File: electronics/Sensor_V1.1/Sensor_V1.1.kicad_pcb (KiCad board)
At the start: 2 copper layers, 45.9 x 25.6 mm, 34 parts, among them J1 nuclone_small_left, J2 nuclone_small_right, J5 DevBoardUartInput, Q1 DMG1012, Q2 DMG1012, Q3 DMG1012, U1 PPG_sensor, U2 reference_sot23-3, U3 MCP6541

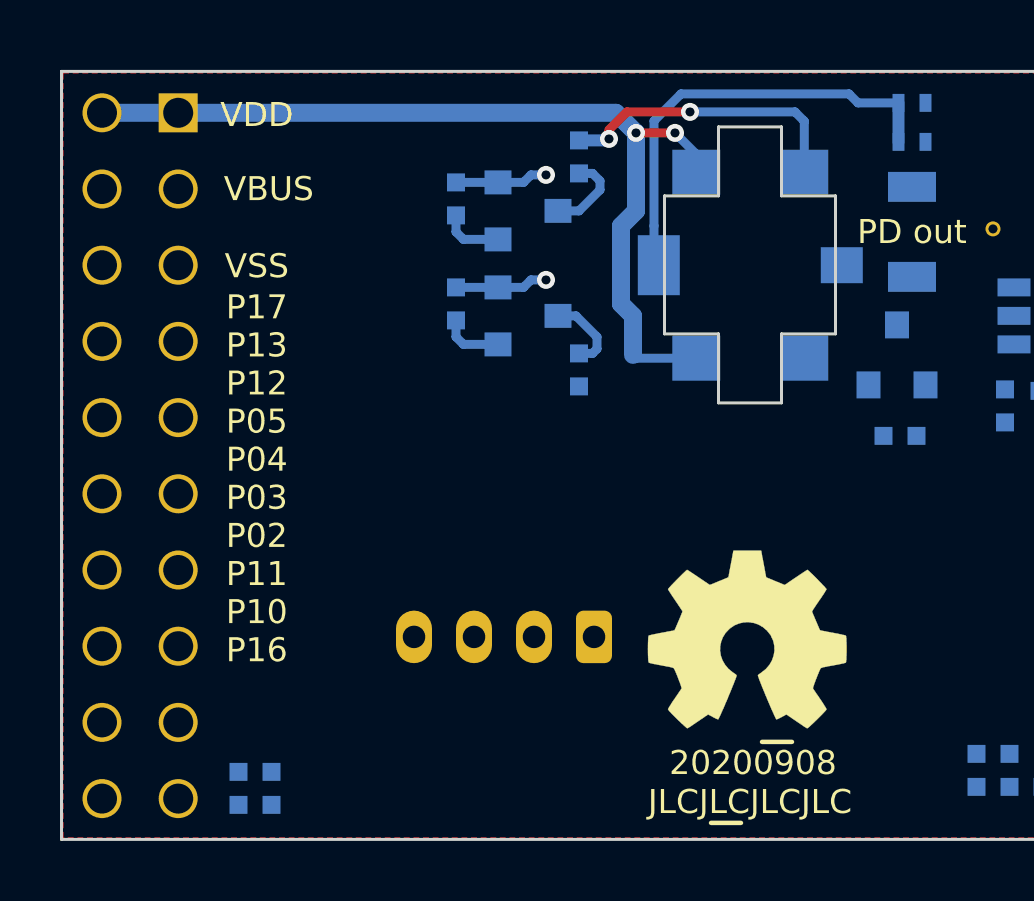
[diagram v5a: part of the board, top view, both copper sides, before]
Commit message: updated layout and started with starground/VDDA
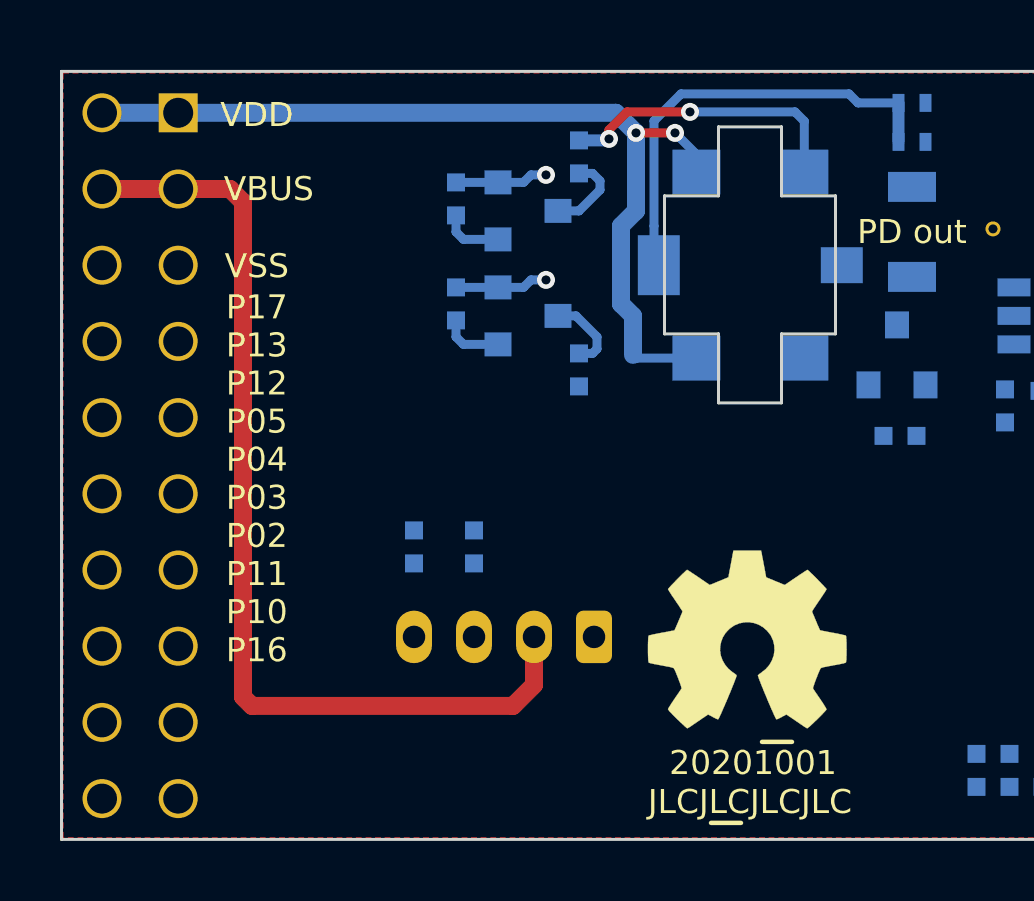
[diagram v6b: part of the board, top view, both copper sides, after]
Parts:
- N2: value 20200908 -> 20201001
- moved R2 11.3 mm to (75.9, 89.4), turned to 270 degrees
- moved R1 9.18 mm to (73.9, 89.4), turned to 270 degrees
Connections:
- J2 pad 19: /VDD -> /VDDA
- J2 pad 20: /VDD -> /VDDA
- JP1 pad 1: /VDD -> /VDDA
- R1 pad 2: Net-(J5-Pad3) -> Net-(J5-Pad4)
- R2 pad 2: Net-(J5-Pad4) -> Net-(J5-Pad3)
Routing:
- net /VBUS: track 0.00 -> 33.1 mm
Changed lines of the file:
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@@
     (thickness 1.6)
     (drawings 57)
-    (tracks 59)
+    (tracks 67)
     (zones 0)
     (modules 34)
@@
   )
   (setup
-    (last_trace_width 0.3)
+    (last_trace_width 0.6)
     (user_trace_width 0.15)
     (user_trace_width 0.2)
@@
   )
   (module SquantorRcl:R_0402_hand (layer B.Cu)
-    (at 68.6 98)
+    (at 75.9 89.4 270)
     (descr "Resistor SMD 0402, reflow soldering, Vishay (see dcrcw.pdf)")
     (tags "resistor 0402")
     (attr smd)
-    (fp_text reference R2 (at 2 0) (layer B.SilkS)
-      (effects (font (size 1 1) (thickness 0.15)) (justify mirror))
-    )
-    (fp_text value 100 (at 0 -1.8) (layer B.Fab)
+    (fp_text reference R2 (at 2 0.2 90) (layer B.SilkS)
+      (effects (font (size 1 1) (thickness 0.15)) (justify mirror))
+    )
+    (fp_text value 100 (at 0 -1.8 90) (layer B.Fab)
       (effects (font (size 1 1) (thickness 0.15)) (justify mirror))
     )
@@
     (fp_line (start -0.1 -0.2) (end -0.1 0.2) (layer B.SilkS) (width 0.15))
     (fp_line (start 0 0.2) (end 0 -0.2) (layer B.SilkS) (width 0.15))
-    (pad 2 smd rect (at 0.55 0) (size 0.6 0.6) (layers B.Cu B.Paste B.Mask)
-      (net 6 "Net-(J5-Pad4)"))
-    (pad 1 smd rect (at -0.55 0) (size 0.6 0.6) (layers B.Cu B.Paste B.Mask)
+    (pad 2 smd rect (at 0.55 0 270) (size 0.6 0.6) (layers B.Cu B.Paste B.Mask)
+      (net 7 "Net-(J5-Pad3)"))
+    (pad 1 smd rect (at -0.55 0 270) (size 0.6 0.6) (layers B.Cu B.Paste B.Mask)
       (net 9 /UART_TX))
     (model ${KISYS3DMOD}/Resistor_SMD.3dshapes/R_0402_1005Metric.step
@@
   )
   (module SquantorRcl:R_0402_hand (layer B.Cu)
-    (at 68.6 96.9)
+    (at 73.9 89.4 270)
     (descr "Resistor SMD 0402, reflow soldering, Vishay (see dcrcw.pdf)")
     (tags "resistor 0402")
     (attr smd)
-    (fp_text reference R1 (at 2 0.1) (layer B.SilkS)
-      (effects (font (size 1 1) (thickness 0.15)) (justify mirror))
-    )
-    (fp_text value 100 (at 0 -1.8) (layer B.Fab)
+    (fp_text reference R1 (at 2 -0.1 90) (layer B.SilkS)
+      (effects (font (size 1 1) (thickness 0.15)) (justify mirror))
+    )
+    (fp_text value 100 (at 0 -1.8 90) (layer B.Fab)
       (effects (font (size 1 1) (thickness 0.15)) (justify mirror))
     )
@@
     (fp_line (start -0.1 -0.2) (end -0.1 0.2) (layer B.SilkS) (width 0.15))
     (fp_line (start 0 0.2) (end 0 -0.2) (layer B.SilkS) (width 0.15))
-    (pad 2 smd rect (at 0.55 0) (size 0.6 0.6) (layers B.Cu B.Paste B.Mask)
-      (net 7 "Net-(J5-Pad3)"))
-    (pad 1 smd rect (at -0.55 0) (size 0.6 0.6) (layers B.Cu B.Paste B.Mask)
+    (pad 2 smd rect (at 0.55 0 270) (size 0.6 0.6) (layers B.Cu B.Paste B.Mask)
+      (net 6 "Net-(J5-Pad4)"))
+    (pad 1 smd rect (at -0.55 0 270) (size 0.6 0.6) (layers B.Cu B.Paste B.Mask)
       (net 8 /UART_RX))
     (model ${KISYS3DMOD}/Resistor_SMD.3dshapes/R_0402_1005Metric.step
@@
       (net 11 /PD_BIAS))
     (pad 1 smd rect (at -0.45 0 180) (size 0.4 0.6) (layers B.Cu B.Mask)
-      (net 3 /VDD))
+      (net 4 /VDDA))
     (model Resistors_SMD.3dshapes/R_0402.wrl
       (at (xyz 0 0 0))
@@
       (effects (font (size 1 1) (thickness 0.15)))
     )
-    (fp_text value 20200908 (at 0.8 -0.1) (layer F.SilkS)
+    (fp_text value 20201001 (at 0.8 -0.1) (layer F.SilkS)
       (effects (font (size 0.8 0.8) (thickness 0.15)))
     )
@@
     (fp_line (start -12.7 -1.905) (end -12.065 -2.54) (layer B.SilkS) (width 0.15))
     (pad 20 thru_hole circle (at 11.43 1.27 90) (size 1.3 1.3) (drill 1) (layers *.Cu *.Mask)
-      (net 3 /VDD))
+      (net 4 /VDDA))
     (pad 19 thru_hole circle (at 11.43 -1.27 90) (size 1.3 1.3) (drill 1) (layers *.Cu *.Mask)
-      (net 3 /VDD))
+      (net 4 /VDDA))
     (pad 18 thru_hole circle (at 8.89 1.27 90) (size 1.3 1.3) (drill 1) (layers *.Cu *.Mask)
       (net 2 /VSS))
@@
   (gr_line (start 62.15 99.15) (end 108.05 99.15) (layer Edge.Cuts) (width 0.1))
   (gr_line (start 62.15 73.55) (end 62.15 99.15) (layer Edge.Cuts) (width 0.1))
+  (segment (start 77.9 92.4) (end 77.9 94) (width 0.6) (layer F.Cu) (net 1))
+  (segment (start 77.9 94) (end 77.2 94.7) (width 0.6) (layer F.Cu) (net 1))
+  (segment (start 77.2 94.7) (end 68.5 94.7) (width 0.6) (layer F.Cu) (net 1))
+  (segment (start 68.5 94.7) (end 68.2 94.4) (width 0.6) (layer F.Cu) (net 1))
+  (segment (start 68.2 94.4) (end 68.2 77.9) (width 0.6) (layer F.Cu) (net 1))
+  (segment (start 67.77 77.47) (end 66.04 77.47) (width 0.6) (layer F.Cu) (net 1))
+  (segment (start 68.2 77.9) (end 67.77 77.47) (width 0.6) (layer F.Cu) (net 1))
+  (segment (start 66.04 77.47) (end 63.5 77.47) (width 0.6) (layer F.Cu) (net 1))
   (segment (start 76.7 80.75) (end 77.55 80.75) (width 0.3) (layer B.Cu) (net 2))
   (via (at 78.3 80.5) (size 0.6) (drill 0.3) (layers F.Cu B.Cu) (net 2))

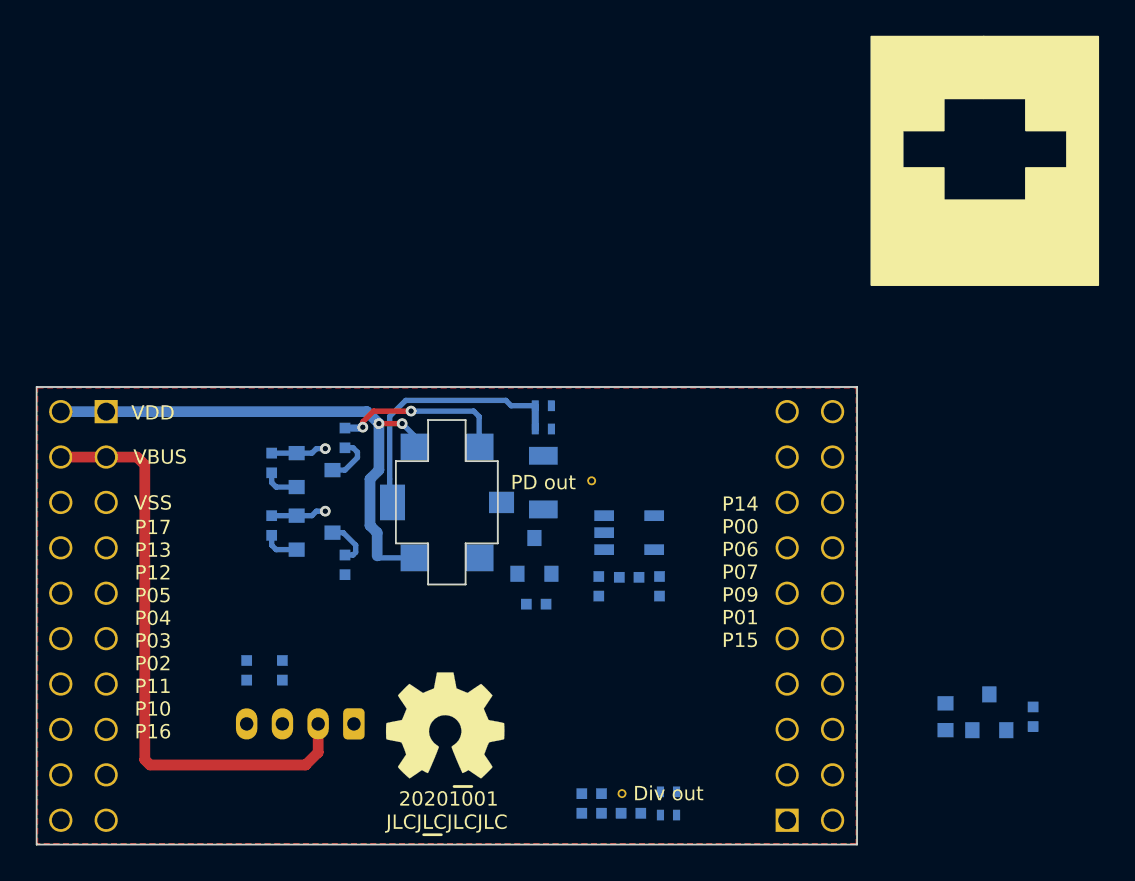
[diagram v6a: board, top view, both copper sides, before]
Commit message: WIP PCB labels
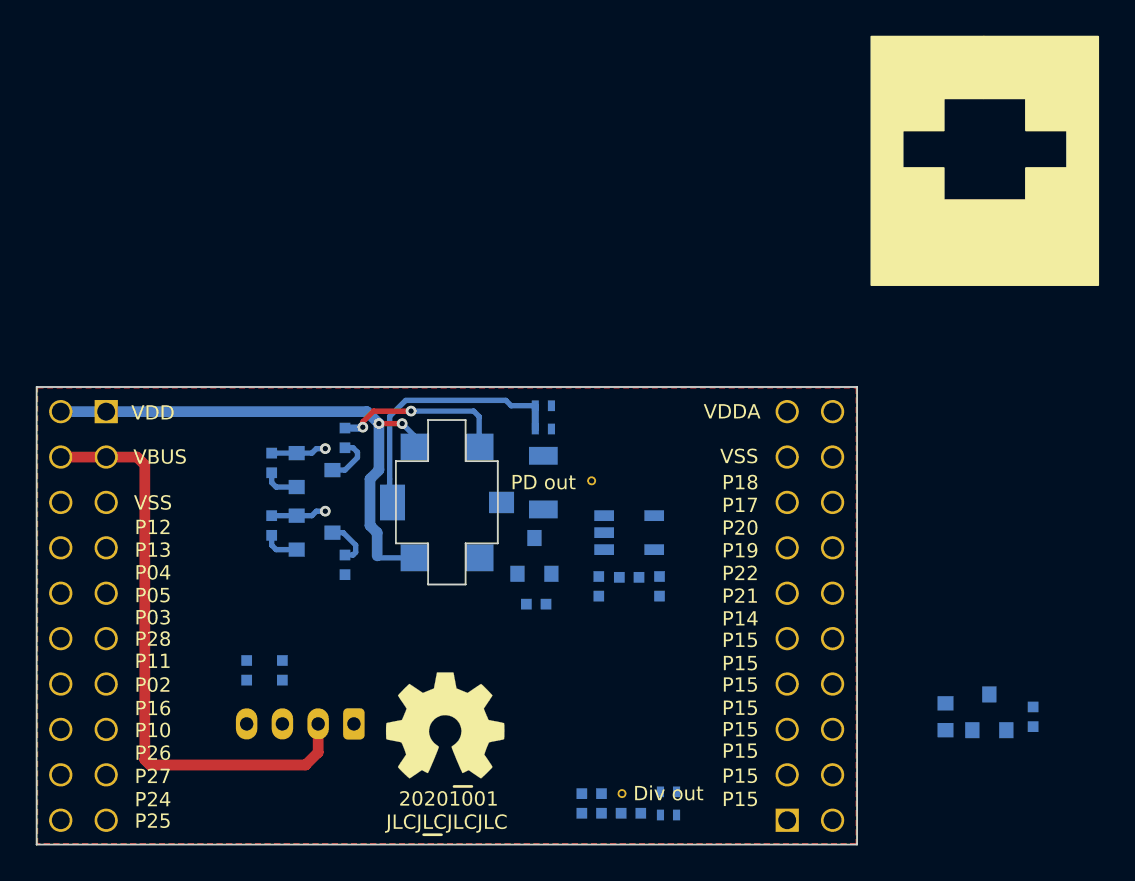
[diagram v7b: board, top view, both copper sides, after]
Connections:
- net Net-(J1-Pad12) renamed /PIO_3
- net Net-(J1-Pad14) renamed /PIO_11
- net Net-(J2-Pad13) renamed /PIO0_19
- net Net-(J2-Pad14) renamed /PIO0_20
- net Net-(J2-Pad15) renamed /PIO0_17
- net Net-(J2-Pad16) renamed /PIO0_18
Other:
- board text added: "P18"
- board text added: "P19"
- board text added: "P20"
- board text added: "P21"
- board text added: "P22"
- board text added: "P24"
- board text added: "P25"
- board text added: "P26"
- board text added: "P27"
- board text added: "P28"
- board text added: "VDDA"
- board text removed: "P00"
- board text removed: "P01"
- board text removed: "P06"
- board text removed: "P07"
- board text removed: "P08"
- board text removed: "P09"

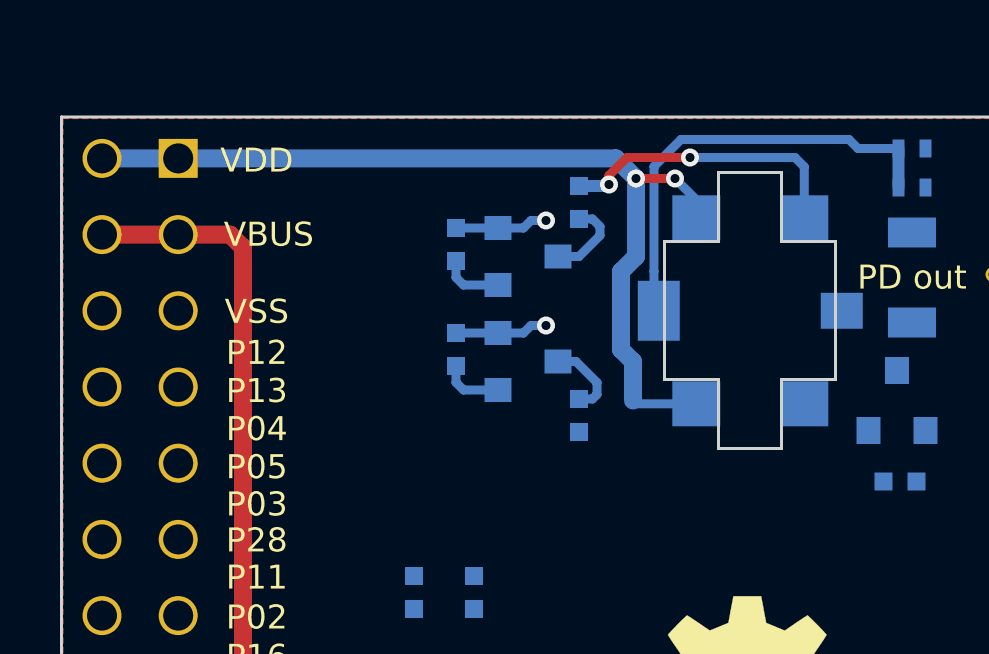
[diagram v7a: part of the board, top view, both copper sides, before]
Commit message: added PD net ties, more ties needed
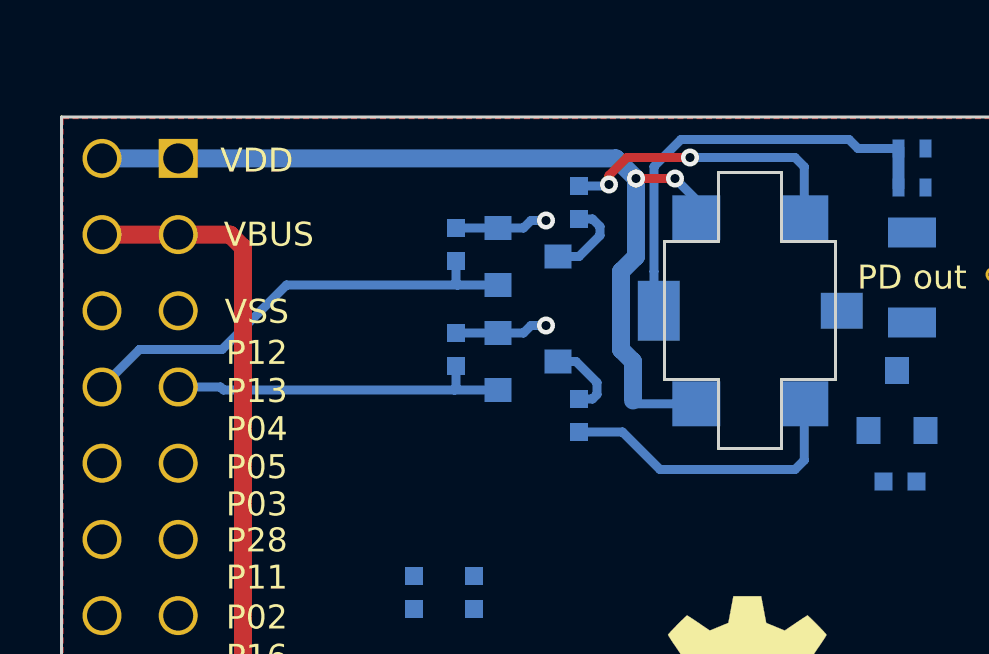
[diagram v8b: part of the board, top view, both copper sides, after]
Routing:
- net /LED2_EN: track 2.05 -> 15.4 mm
- net /LED1: track 0.00 -> 10.0 mm
- net /LED1_EN: track 2.05 -> 11.5 mm
